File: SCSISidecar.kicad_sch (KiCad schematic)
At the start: 83 parts, among them J2 SCSI, J3 Conn_01x03, J4 Conn_01x03, J5 LED, J6 A/B, J7 Conn_01x02, SW1 ENABLE, U1 PAL16L8, U10 PAL16L8, U11 CXO_DIP14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

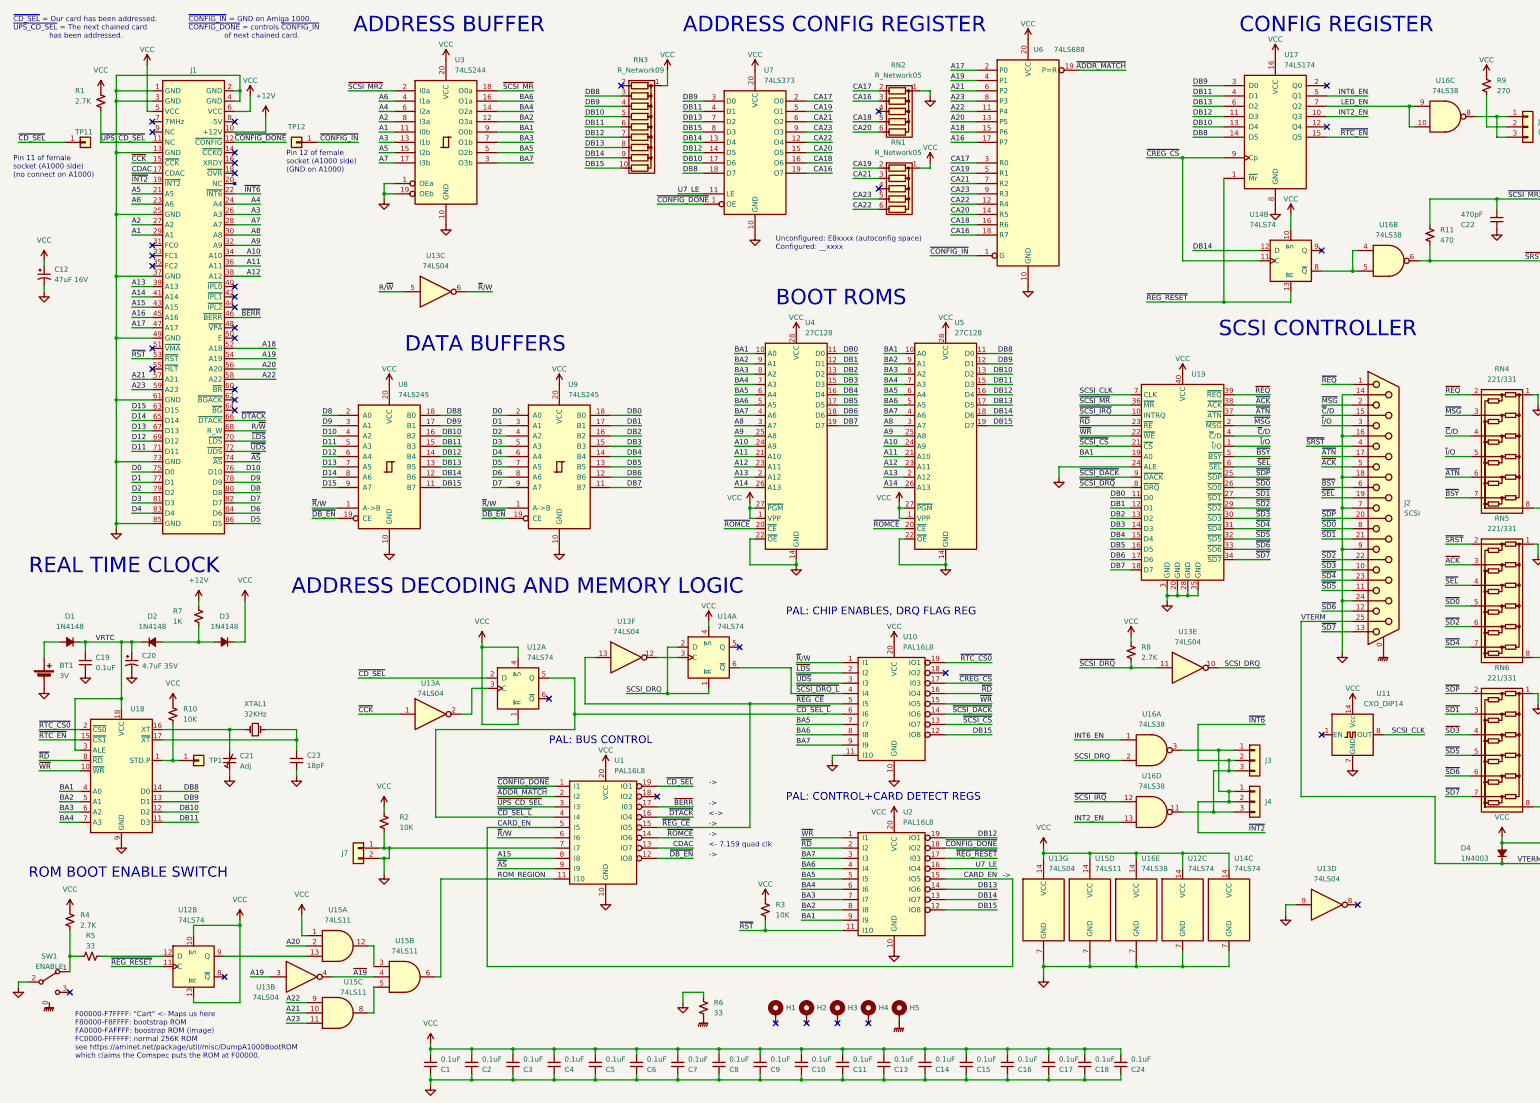
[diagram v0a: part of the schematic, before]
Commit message: add readme, add right angle connector board, layout changes to accommodate it
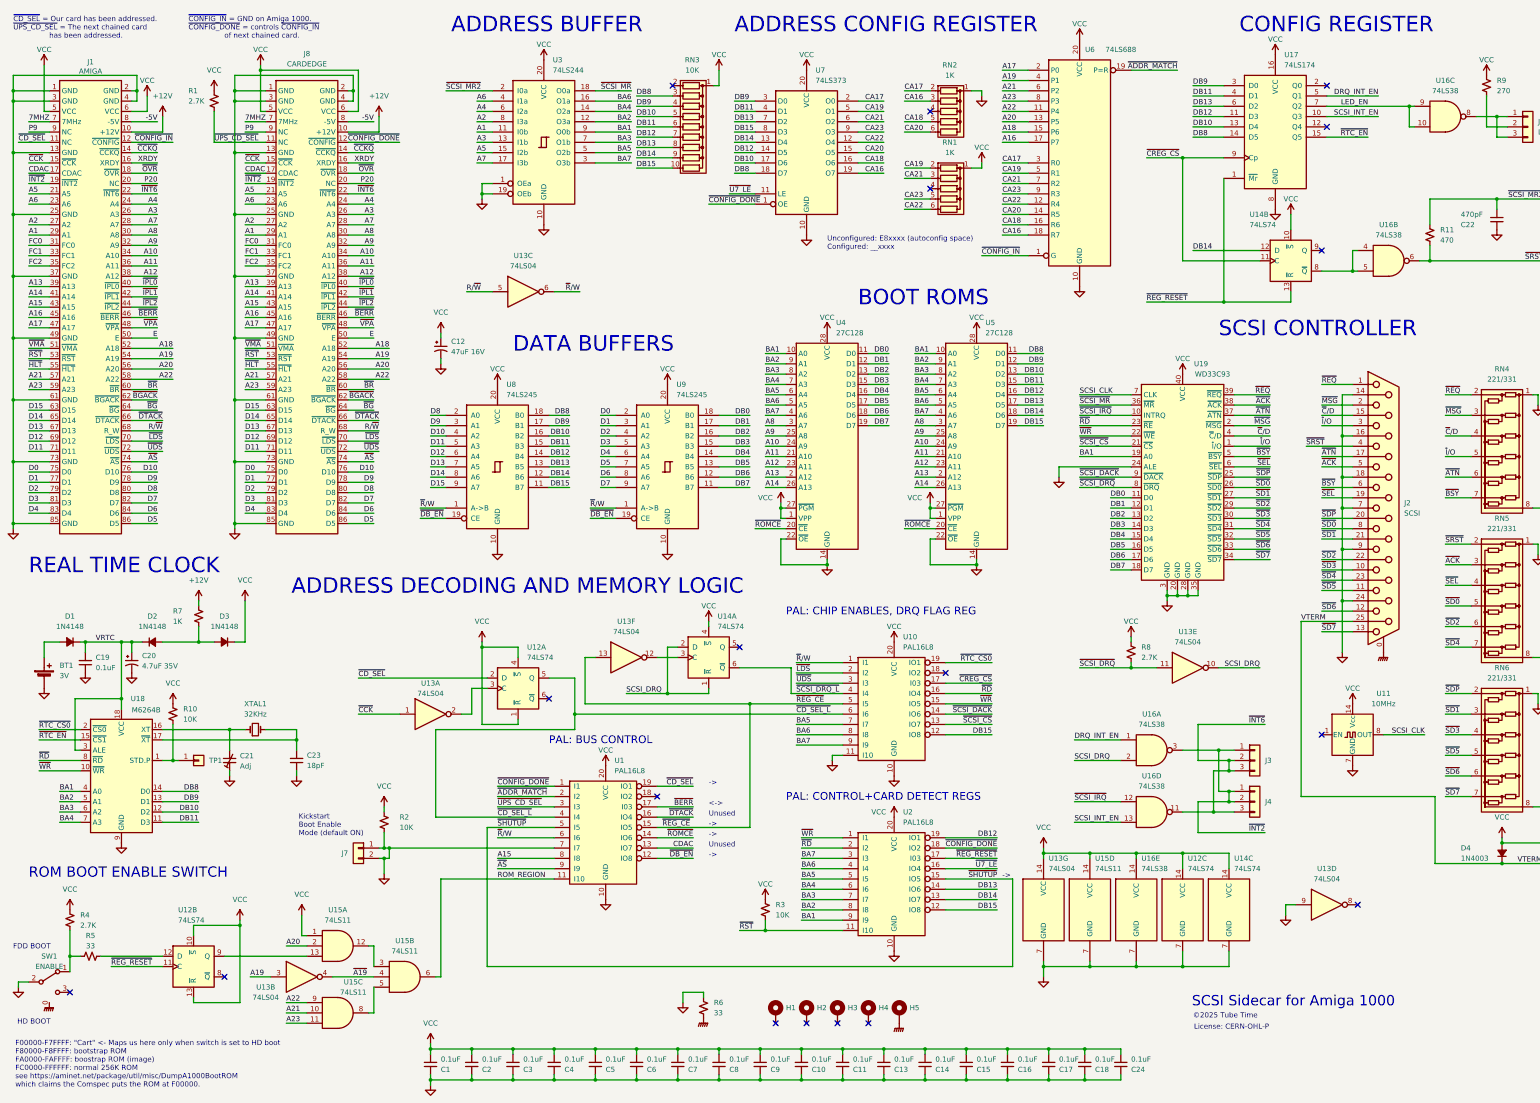
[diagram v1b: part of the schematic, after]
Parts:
- removed TP11, TP12: Conn_01x01, Connector_PinHeader_2.54mm:PinHeader_1x01_P2.54mm_Vertical, symbol Connector_Generic:Conn_01x01
- added J8: CARDEDGE, Conn:PinHeader_2x43_P2.54mm_Vertical, symbol connectors:Conn_Amiga1000
- BT1: MPN (none) -> Keystone 104
- J1: value ~ -> AMIGA; footprint Conn:EDAC_345-086-541 -> Conn:TE_1-5530843-0; MPN (none) -> TE 1-5530843-0 or equiv
- RN1, RN2: value R_Network05 -> 1K
- RN3: value R_Network09 -> 10K
- SW1: MPN (none) -> 7101J1AV2QE2 or equiv
- U11: value CXO_DIP14 -> 10MHz; MPN (none) -> ECS-100AX-100 or equiv
- U18: value ~ -> M6264B
- U19: value ~ -> WD33C93
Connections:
- net +12V: now also J8.10 (+12V)
- net A1: now also J8.29 (A1)
- net A10: now also J8.34 (A10)
- net A11: now also J8.36 (A11)
- net A12: now also J8.38 (A12)
- net A13: now also J8.39 (A13)
- net A14: now also J8.41 (A14)
- net A15: now also J8.43 (A15)
- net A16: now also J8.45 (A16)
- net A17: now also J8.47 (A17)
- net A18: now also J8.52 (A18)
- net A19: now also J8.54 (A19)
- net A2: now also J8.27 (A2)
- net A20: now also J8.56 (A20)
- net A21: now also J8.57 (A21)
- net A22: now also J8.58 (A22)
- net A23: now also J8.59 (A23)
- net A3: now also J8.26 (A3)
- net A4: now also J8.24 (A4)
- net A5: now also J8.21 (A5)
- net A6: now also J8.23 (A6)
- net A7: now also J8.28 (A7)
- net A8: now also J8.30 (A8)
- net A9: now also J8.32 (A9)
- net CDAC: now also J8.17 (CDAC)
- net D0: now also J8.75 (D0)
- net D1: now also J8.77 (D1)
- net D10: now also J8.76 (D10)
- net D11: now also J8.71 (D11)
- net D12: now also J8.69 (D12)
- net D13: now also J8.67 (D13)
- net D14: now also J8.65 (D14)
- net D15: now also J8.63 (D15)
- net D2: now also J8.79 (D2)
- net D3: now also J8.81 (D3)
- net D4: now also J8.83 (D4)
- net D5: now also J8.86 (D5)
- net D6: now also J8.84 (D6)
- net D7: now also J8.82 (D7)
- net D8: now also J8.80 (D8)
- net D9: now also J8.78 (D9)
- net GND: now also J8.1 (GND), J8.13 (GND), J8.2 (GND), J8.25 (GND), J8.3 (GND), J8.37 (GND), J8.4 (GND), J8.49 (GND), J8.61 (GND), J8.73 (GND), J8.85 (GND)
- net R/~{W}: now also J8.68 (R_W)
- net VCC: now also J8.5 (VCC), J8.6 (VCC)
- net ~{AS}: now also J8.74 (~{AS})
- net ~{BERR}: now also J8.46 (~{BERR})
- net ~{CCK}: now also J8.15 (~{CCK})
- net ~{CD_SEL}: now also J1.11 (NC)
- net ~{CONFIG_DONE}: now also J8.12 (~{CONFIG}); no longer J1.12 (~{CONFIG})
- net ~{CONFIG_IN}: now also J1.12 (~{CONFIG})
- net ~{DTACK}: now also J8.66 (~{DTACK})
- net ~{INT2}: now also J8.19 (~{INT2})
- net ~{INT6}: now also J8.22 (~{INT6})
- net ~{LDS}: now also J8.70 (~{LDS})
- net ~{RST}: now also J8.53 (~{RST})
- net ~{UDS}: now also J8.72 (~{UDS})
- net ~{UPS_CD_SEL}: now also J8.11 (NC); no longer J1.11 (NC)
- net ~{CCKQ}: now reaches J1.14 (~{CCKQ})
- net ~{CCKQ}: now also J8.14 (~{CCKQ})
- net XRDY: now reaches J1.16 (XRDY)
- net XRDY: now also J8.16 (XRDY)
- net ~{OVR}: now reaches J1.18 (~{OVR})
- net ~{OVR}: now also J8.18 (~{OVR})
- net P20: now reaches J1.20 (NC)
- net P20: now also J8.20 (NC)
- net FC0: now reaches J1.31 (FC0)
- net FC0: now also J8.31 (FC0)
- net FC1: now reaches J1.33 (FC1)
- net FC1: now also J8.33 (FC1)
- net FC2: now reaches J1.35 (FC2)
- net FC2: now also J8.35 (FC2)
- net ~{IPL0}: now reaches J1.40 (~{IPL0})
- net ~{IPL0}: now also J8.40 (~{IPL0})
- net ~{IPL1}: now reaches J1.42 (~{IPL1})
- net ~{IPL1}: now also J8.42 (~{IPL1})
- net ~{IPL2}: now reaches J1.44 (~{IPL2})
- net ~{IPL2}: now also J8.44 (~{IPL2})
- net ~{VPA}: now reaches J1.48 (~{VPA})
- net ~{VPA}: now also J8.48 (~{VPA})
- net E: now reaches J1.50 (E)
- net E: now also J8.50 (E)
- net ~{VMA}: now reaches J1.51 (~{VMA})
- net ~{VMA}: now also J8.51 (~{VMA})
- net ~{HLT}: now reaches J1.55 (~{HLT})
- net ~{HLT}: now also J8.55 (~{HLT})
- net ~{BR}: now reaches J1.60 (~{BR})
- net ~{BR}: now also J8.60 (~{BR})
- net ~{BGACK}: now reaches J1.62 (~{BGACK})
- net ~{BGACK}: now also J8.62 (~{BGACK})
- net ~{BG}: now reaches J1.64 (~{BG})
- net ~{BG}: now also J8.64 (~{BG})
- net 7MHZ: now reaches J1.7 (7MHz)
- net 7MHZ: now also J8.7 (7MHz)
- net -5V: now reaches J1.8 (-5V)
- net -5V: now also J8.8 (-5V)
- net P9: now reaches J1.9 (NC)
- net P9: now also J8.9 (NC)
- net CARD_EN renamed ~{SHUTUP}
- net INT2_EN renamed SCSI_INT_EN
- net INT6_EN renamed DRQ_INT_EN
- net U7_LE renamed ~{U7_LE}
- no-connect marks 37 -> 18
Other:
- note added: "F00000-F7FFFF: "Cart" <- Maps us here only when switch is set to HD boot F80000-F8FFFF: bootstrap ROM FA0000-FAFFFF: boostrap ROM (image) FC0000-FFFFFF: normal 256K ROM see https://aminet.net/package/util/misc/DumpA1000BootROM which claims the Comspec puts the ROM at F00000."
- note added: "FDD BOOT"
- note added: "HD BOOT"
- note added: "Kickstart Boot Enable Mode (default ON)"
- note added: "License: CERN-OHL-P"
- note added: "SCSI Sidecar for Amiga 1000"
- note added: "Unused"
- note added: "©2025 Tube Time"
- note removed: "<- 7.159 quad clk"
- note removed: "F00000-F7FFFF: "Cart" <- Maps us here F80000-F8FFFF: bootstrap ROM FA0000-FAFFFF: boostrap ROM (image) FC0000-FFFFFF: normal 256K ROM see https://aminet.net/package/util/misc/DumpA1000BootROM which claims the Comspec puts the ROM at F00000."
- note removed: "Pin 11 of female socket (A1000 side) (no connect on A1000)"
- note removed: "Pin 12 of female socket (A1000 side) (GND on A1000)"
- moved on the sheet: C12, R1, RN1, RN2, RN3, U13C, U3, U4, U5, U6, U7, U8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

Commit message: Add new photos, 33C93 note
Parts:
- RN1, RN2: MPN (none) -> 4606X-101-102LF
- RN3: MPN (none) -> 4610X-101-103LF
- SW1: MPN 7101J1AV2QE2 or equiv -> 7101J1AV2QE2, 300SP1J1BLKM7QE, or equiv
- U18: value M6264B -> M6242B; MPN (none) -> M6242B, RTC-72421, or equivalent
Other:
- note added: "DEFAULT A (2-3)"
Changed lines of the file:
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@@
 		)
 	)
+	(text "DEFAULT\nA (2-3)"
+		(exclude_from_sim no)
+		(at 399.288 213.868 0)
+		(effects
+			(font
+				(size 1.27 1.27)
+			)
+		)
+	)
 	(text "PAL: BUS CONTROL"
 		(exclude_from_sim no)
@@
 			)
 		)
+		(property "MPN" "4610X-101-103LF"
+			(at 181.61 41.91 90)
+			(effects
+				(font
+					(size 1.27 1.27)
+				)
+				(hide yes)
+			)
+		)
 		(pin "1"
 		)
@@
 		)
 		(property "Value" "WD33C93"
-			(at 309.626 102.87 0)
+			(at 305.308 102.87 0)
 			(effects
 				(font
 					(size 1.27 1.27)
 				)
+				(justify left)
 			)
 		)
@@
 			)
 		)
+		(property "MPN" "4606X-101-102LF"
+			(at 245.11 38.1 90)
+			(effects
+				(font
+					(size 1.27 1.27)
+				)
+				(hide yes)
+			)
+		)
 		(pin "1"
 		)
@@
 			)
 		)
-		(property "Value" "M6264B"
+		(property "Value" "M6242B"
 			(at 46.736 185.674 0)
 			(effects
@@
 			)
 		)
+		(property "MPN" "M6242B, RTC-72421, or equivalent"
+			(at 33.02 187.96 0)
+			(effects
+				(font
+					(size 1.27 1.27)
+				)
+				(hide yes)
+			)
+		)
 		(pin "1"
 		)
@@
 			)
 		)
-		(property "MPN" "7101J1AV2QE2 or equiv"
+		(property "MPN" "7101J1AV2QE2, 300SP1J1BLKM7QE, or equiv"
 			(at 22.86 252.73 0)
 			(effects
@@
 			(effects
 				(font
+					(size 1.27 1.27)
+				)
+				(hide yes)
+			)
+		)
+		(property "MPN" "4606X-101-102LF"
+			(at 245.11 57.15 90)
+			(effects
+				(font
